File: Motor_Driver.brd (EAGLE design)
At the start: 68.6 x 30.1 mm, 20 parts, among them T1 2N3904, T2 2N3904

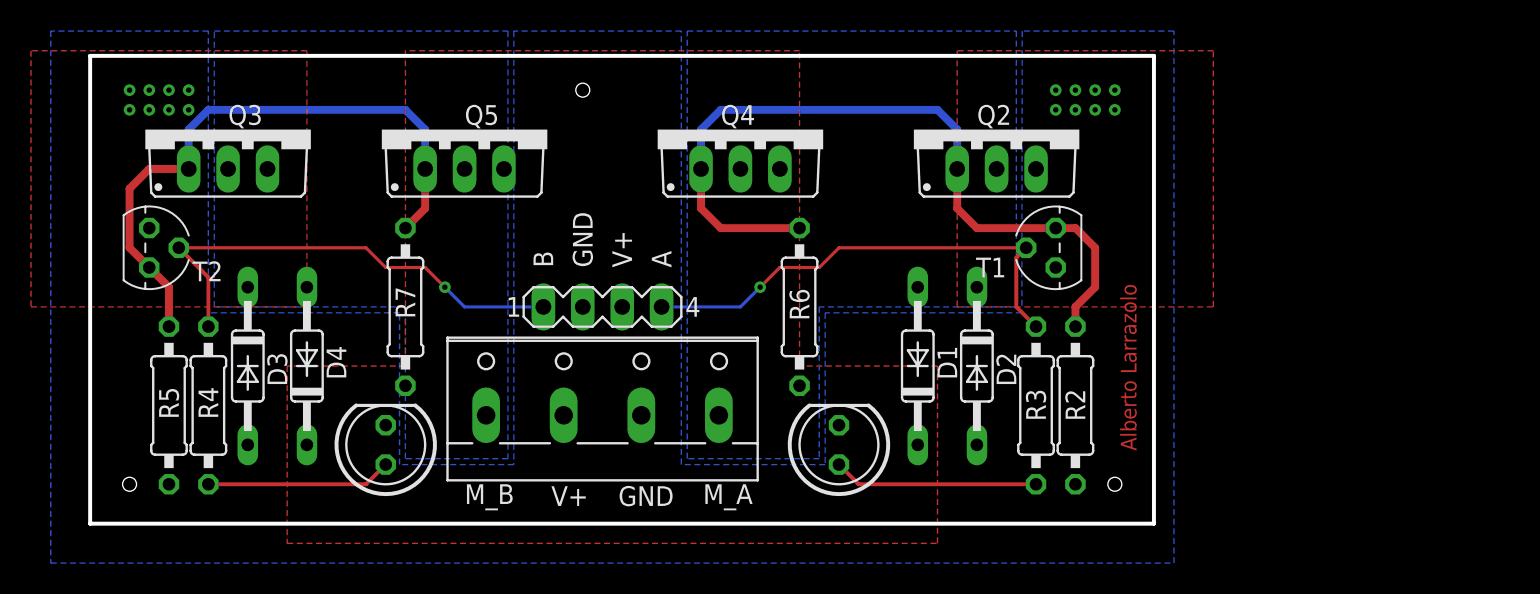
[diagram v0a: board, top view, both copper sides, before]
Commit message: Increased space between MOSFETs to allow for proper heatsink size
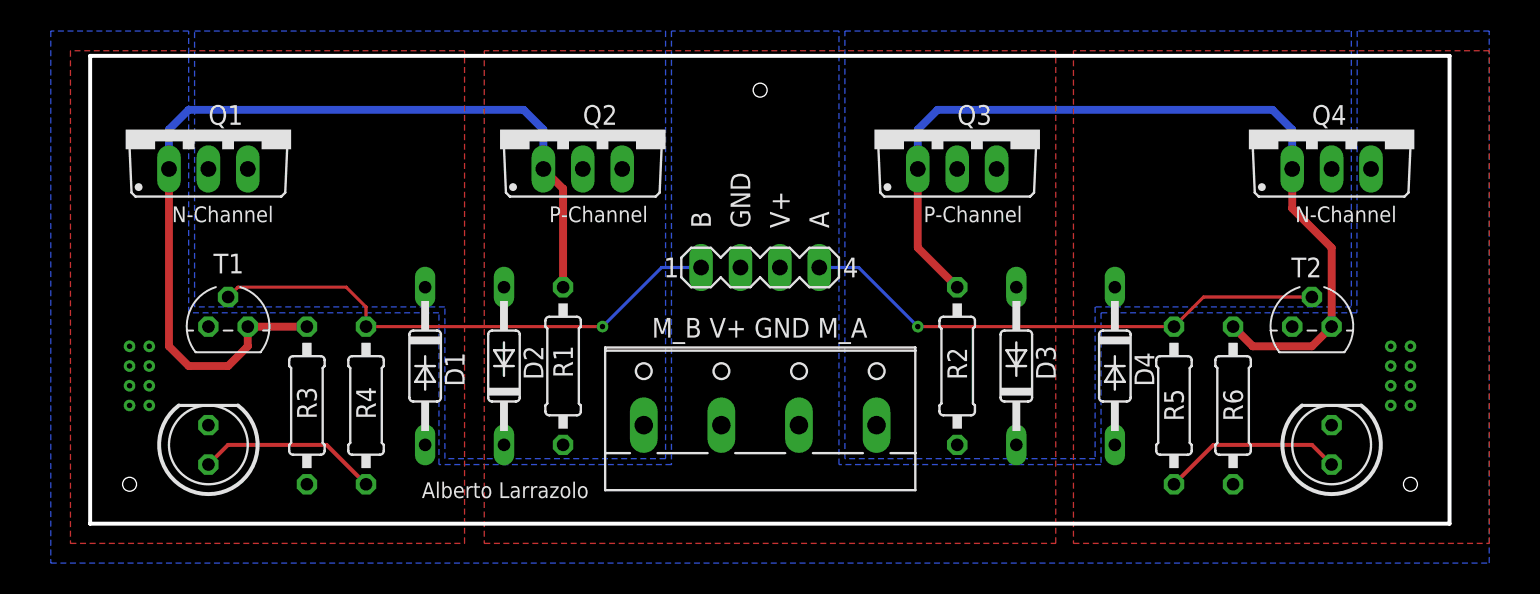
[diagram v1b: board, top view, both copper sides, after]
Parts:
- removed Q5: (no value), transistor-power:TO220BV
- removed R7: 1k, resistor:0207/10
- removed X2: (no value), con-wago-500:W237-4
- added Q1: (no value), transistor-power:TO220BV
- added R1: 1k, resistor:0207/10
- added X1: M_B V+ GND M_A, MyParts:W237-4
- R2, R5: value 10k -> 1k
- R3, R6: value 1k -> 10k
- SV1: value (none) -> INPUT_HEADER; device con-lstb:MA04-1 -> MyParts:MA04-1
- moved T2 75.1 mm to (78.7, 12.7), turned to 0 degrees
- moved R5 64.8 mm to (69.8, 7.62)
- moved LED2 61.0 mm to (80.0, 5.08)
- moved T1 53.6 mm to (8.89, 12.7), turned to 0 degrees
- moved D4 52.1 mm to (66.0, 10.2), turned to 270 degrees
- moved D3 49.5 mm to (59.7, 10.2), turned to 90 degrees
- moved Q3 47.0 mm to (55.9, 25.4)
- moved R3 47.0 mm to (14.0, 7.62)
- moved LED1 40.6 mm to (7.62, 5.08)
- moved Q4 38.1 mm to (80.0, 25.4)
- moved D1 31.8 mm to (21.6, 10.2), turned to 270 degrees
- moved D2 30.5 mm to (26.7, 10.2), turned to 90 degrees
- moved R6 28.7 mm to (73.7, 7.62), turned to 90 degrees
- moved Q2 26.7 mm to (31.8, 25.4)
- moved SV1 10.5 mm to (43.2, 16.5)
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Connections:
- net +12V: now also D2.C, D3.C, Q2.S, Q3.S, R1.2, R2.2, X1.2; no longer D1.C, D4.C, Q4.S, Q5.S, R6.2, R7.2, X2.2
- net DRIVE_A: now also Q3.G, R2.1, R6.2, T2.1; no longer Q2.G, R2.2, R6.1, T1.1
- net DRIVE_B: now also Q1.G, Q2.G, R1.1, R3.2, T1.1; no longer Q3.G, Q5.G, R5.2, R7.1, T2.1
- net GND: now also D1.A, D4.A, Q1.S, Q4.S, R3.1, R6.1, X1.3; no longer D2.A, D3.A, Q2.S, Q3.S, R2.1, R5.1, X2.3
- net INPUT_A: now also R5.2, T2.2; no longer R3.2, T1.2
- net INPUT_B: now also T1.2; no longer T2.2
- net M_DRIVE_A: now also D3.A, D4.C, Q3.D, X1.4; no longer D1.A, D2.C, Q2.D, X2.4
- net M_DRIVE_B: now also D1.C, D2.A, Q1.D, Q2.D, X1.1; no longer D3.C, D4.A, Q3.D, Q5.D, X2.1
- net N$2: now also LED2.A, R5.1; no longer LED1.A, R3.1
- net N$4: now also LED1.A; no longer LED2.A
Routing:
- net DRIVE_B: track 40.0 -> 61.1 mm
- net DRIVE_A: track 50.1 -> 57.5 mm
- net INPUT_B: track 30.8 -> 34.1 mm
- net INPUT_A: track 30.8 -> 34.1 mm
- net N$2: track 13.2 -> 11.7 mm
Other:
- board size 68.6 x 30.1 mm -> 87.6 x 30.1 mm
- board text added: "N-Channel"
- board text added: "P-Channel"

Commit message: Fixed termal relif to allow higher current flow
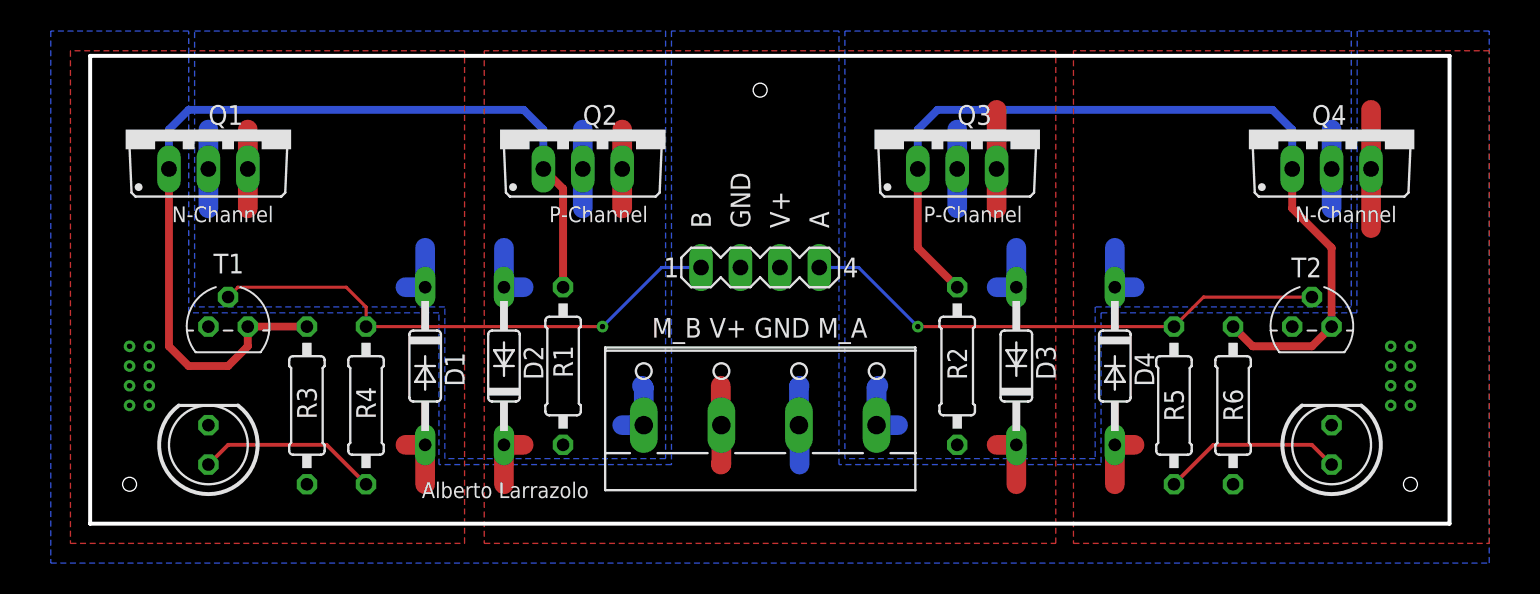
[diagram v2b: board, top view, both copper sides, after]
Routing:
- net GND: track 0.00 -> 25.4 mm
- net +12V: track 0.00 -> 24.2 mm
- net M_DRIVE_B: track 0.00 -> 21.8 mm
- net M_DRIVE_A: track 0.00 -> 21.8 mm
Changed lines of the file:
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@@
 </layers>
 <board>
-<fusionsync huburn="a.cGVyc29uYWw6dWUyYmQxNTYx" projecturn="a.cGVyc29uYWw6dWUyYmQxNTYxIzIwMTcwNTAzNzQ1OTM2NTY" f3durn="urn:adsk.wipprod:dm.lineage:4LoYFpwRT0WNoFuGUnykHQ" pcbguid="78764fb1-ee6b-49c0-b5bc-c6e3655d7beb" lastpulledtime="2019-02-07T21:09:33Z" lastsyncedchangeguid="44b8d85f-1404-02d4-668d-95ffcc52724d"/>
+<fusionsync huburn="a.cGVyc29uYWw6dWUyYmQxNTYx" projecturn="a.cGVyc29uYWw6dWUyYmQxNTYxIzIwMTcwNTAzNzQ1OTM2NTY" f3durn="urn:adsk.wipprod:dm.lineage:4LoYFpwRT0WNoFuGUnykHQ" pcbguid="78764fb1-ee6b-49c0-b5bc-c6e3655d7beb" lastpulledtime="2019-02-07T21:09:33Z" lastsyncedchangeguid="b2fdb641-c53b-a119-a0bc-a5a252d5b16f"/>
 <plain>
 <text x="32.131" y="2.667" size="1.016" layer="21" font="vector" rot="R180">Alberto Larrazolo</text>
@@
 <class number="0" name="default" width="0" drill="0">
 </class>
-<class number="1" name="Motor_Power" width="2.54" drill="0">
+<class number="1" name="Motor_Power" width="1.27" drill="0">
 </class>
 </classes>
@@
 </polygon>
 <contactref element="X1" pad="1"/>
+<wire x1="7.62" y1="22.86" x2="7.62" y2="20.32" width="1.27" layer="16"/>
+<wire x1="7.62" y1="22.86" x2="7.62" y2="25.4" width="1.27" layer="16"/>
+<wire x1="31.75" y1="22.86" x2="31.75" y2="20.32" width="1.27" layer="16"/>
+<wire x1="31.75" y1="22.86" x2="31.75" y2="25.4" width="1.27" layer="16"/>
+<wire x1="35.68" y1="6.35" x2="35.68" y2="8.77" width="1.27" layer="16"/>
+<wire x1="35.68" y1="8.77" x2="35.56" y2="8.89" width="1.27" layer="16"/>
+<wire x1="35.68" y1="6.35" x2="34.29" y2="6.35" width="1.27" layer="16"/>
+<wire x1="21.59" y1="15.24" x2="21.59" y2="17.78" width="1.27" layer="16"/>
+<wire x1="26.67" y1="15.24" x2="27.94" y2="15.24" width="1.27" layer="16"/>
+<wire x1="26.67" y1="15.24" x2="26.67" y2="17.78" width="1.27" layer="16"/>
+<wire x1="21.59" y1="15.24" x2="20.32" y2="15.24" width="1.27" layer="16"/>
 </signal>
 <signal name="M_DRIVE_A" class="1">
@@
 </polygon>
 <contactref element="X1" pad="4"/>
+<wire x1="55.88" y1="22.86" x2="55.88" y2="20.32" width="1.27" layer="16"/>
+<wire x1="55.88" y1="22.86" x2="55.88" y2="25.4" width="1.27" layer="16"/>
+<wire x1="80.01" y1="22.86" x2="80.01" y2="25.4" width="1.27" layer="16"/>
+<wire x1="80.01" y1="22.86" x2="80.01" y2="20.32" width="1.27" layer="16"/>
+<wire x1="50.68" y1="6.35" x2="50.68" y2="8.77" width="1.27" layer="16"/>
+<wire x1="50.68" y1="8.77" x2="50.8" y2="8.89" width="1.27" layer="16"/>
+<wire x1="50.68" y1="6.35" x2="52.07" y2="6.35" width="1.27" layer="16"/>
+<wire x1="66.04" y1="15.24" x2="67.31" y2="15.24" width="1.27" layer="16"/>
+<wire x1="66.04" y1="15.24" x2="66.04" y2="17.78" width="1.27" layer="16"/>
+<wire x1="59.69" y1="15.24" x2="58.42" y2="15.24" width="1.27" layer="16"/>
+<wire x1="59.69" y1="15.24" x2="59.69" y2="17.78" width="1.27" layer="16"/>
 </signal>
 <signal name="+12V">
@@
 <contactref element="D2" pad="C"/>
 <contactref element="X1" pad="2"/>
+<wire x1="34.29" y1="22.86" x2="34.29" y2="20.32" width="1.27" layer="1"/>
+<wire x1="34.29" y1="22.86" x2="34.29" y2="25.4" width="1.27" layer="1"/>
+<wire x1="58.42" y1="22.86" x2="58.42" y2="20.32" width="1.27" layer="1"/>
+<wire x1="58.42" y1="22.86" x2="58.42" y2="26.67" width="1.27" layer="1"/>
+<wire x1="40.68" y1="6.35" x2="40.64" y2="6.39" width="1.27" layer="1"/>
+<wire x1="40.64" y1="6.39" x2="40.64" y2="8.89" width="1.27" layer="1"/>
+<wire x1="40.68" y1="6.35" x2="40.68" y2="3.85" width="1.27" layer="1"/>
+<wire x1="40.68" y1="3.85" x2="40.64" y2="3.81" width="1.27" layer="1"/>
+<wire x1="26.67" y1="5.08" x2="26.67" y2="2.54" width="1.27" layer="1"/>
+<wire x1="26.67" y1="5.08" x2="27.94" y2="5.08" width="1.27" layer="1"/>
+<wire x1="59.69" y1="5.08" x2="58.42" y2="5.08" width="1.27" layer="1"/>
+<wire x1="59.69" y1="5.08" x2="59.69" y2="2.54" width="1.27" layer="1"/>
 </signal>
 <signal name="GND">
@@
 <via x="83.82" y="11.43" extent="1-16" drill="0.35"/>
 <contactref element="X1" pad="3"/>
+<wire x1="82.55" y1="22.86" x2="82.55" y2="19.05" width="1.27" layer="1"/>
+<wire x1="82.55" y1="22.86" x2="82.55" y2="26.67" width="1.27" layer="1"/>
+<wire x1="10.16" y1="22.86" x2="10.16" y2="20.32" width="1.27" layer="1"/>
+<wire x1="10.16" y1="22.86" x2="10.16" y2="25.4" width="1.27" layer="1"/>
+<wire x1="45.68" y1="6.35" x2="45.68" y2="8.85" width="1.27" layer="16"/>
+<wire x1="45.68" y1="8.85" x2="45.72" y2="8.89" width="1.27" layer="16"/>
+<wire x1="45.68" y1="6.35" x2="45.72" y2="6.31" width="1.27" layer="16"/>
+<wire x1="45.72" y1="6.31" x2="45.72" y2="3.81" width="1.27" layer="16"/>
+<wire x1="21.59" y1="5.08" x2="21.59" y2="2.54" width="1.27" layer="1"/>
+<wire x1="21.59" y1="5.08" x2="20.32" y2="5.08" width="1.27" layer="1"/>
+<wire x1="66.04" y1="5.08" x2="66.04" y2="2.54" width="1.27" layer="1"/>
+<wire x1="66.04" y1="5.08" x2="67.31" y2="5.08" width="1.27" layer="1"/>
 </signal>
 <signal name="INPUT_A">

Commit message: Fixed a trace that had shallow angle.
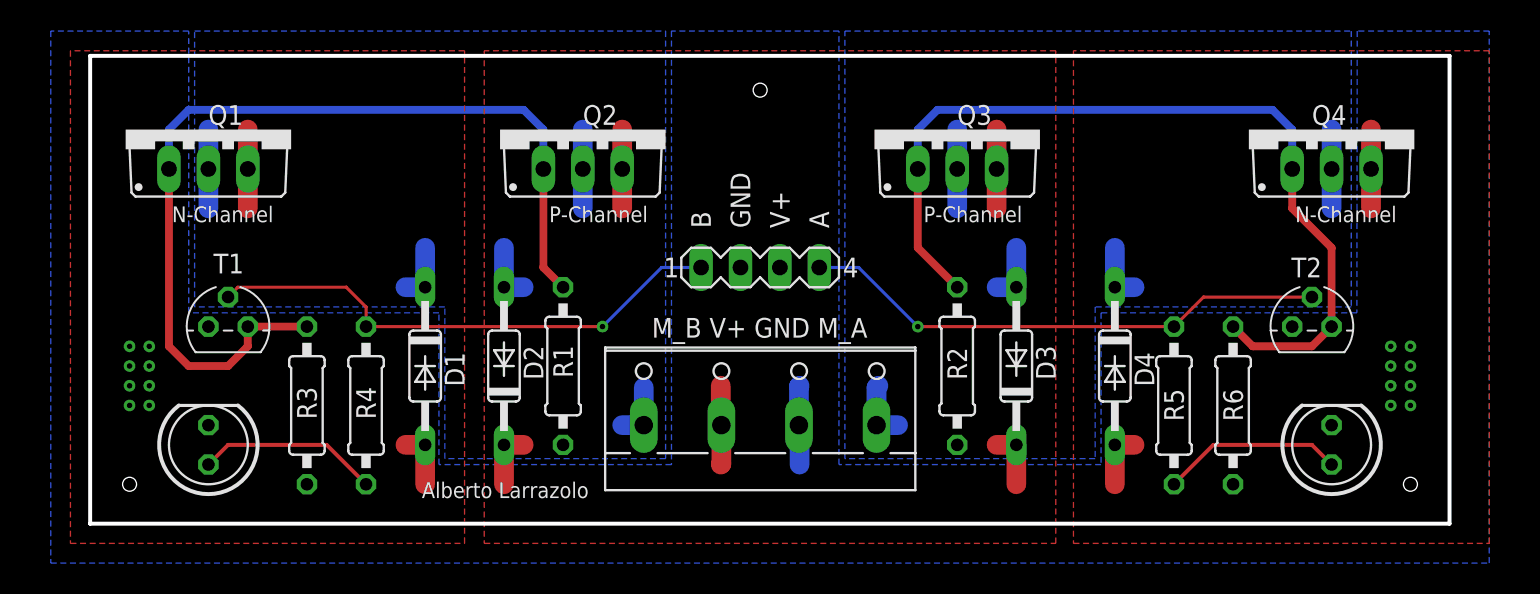
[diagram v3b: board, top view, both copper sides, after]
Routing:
- net GND: track 25.4 -> 22.9 mm
- net +12V: track 24.2 -> 22.9 mm
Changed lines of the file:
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@@
 <contactref element="Q1" pad="G"/>
 <contactref element="Q2" pad="G"/>
-<wire x1="29.21" y1="22.86" x2="30.48" y2="21.59" width="0.508" layer="1"/>
-<wire x1="30.48" y1="21.59" x2="30.48" y2="15.24" width="0.508" layer="1"/>
+<wire x1="29.21" y1="22.86" x2="29.21" y2="16.51" width="0.508" layer="1"/>
+<wire x1="29.21" y1="16.51" x2="30.48" y2="15.24" width="0.508" layer="1"/>
 <wire x1="6.35" y1="26.67" x2="5.08" y2="25.4" width="0.508" layer="16"/>
 <wire x1="5.08" y1="25.4" x2="5.08" y2="22.86" width="0.508" layer="16"/>
@@
 <wire x1="31.75" y1="22.86" x2="31.75" y2="25.4" width="1.27" layer="16"/>
 <wire x1="35.68" y1="6.35" x2="35.68" y2="8.77" width="1.27" layer="16"/>
-<wire x1="35.68" y1="8.77" x2="35.56" y2="8.89" width="1.27" layer="16"/>
 <wire x1="35.68" y1="6.35" x2="34.29" y2="6.35" width="1.27" layer="16"/>
 <wire x1="21.59" y1="15.24" x2="21.59" y2="17.78" width="1.27" layer="16"/>
@@
 <wire x1="34.29" y1="22.86" x2="34.29" y2="25.4" width="1.27" layer="1"/>
 <wire x1="58.42" y1="22.86" x2="58.42" y2="20.32" width="1.27" layer="1"/>
-<wire x1="58.42" y1="22.86" x2="58.42" y2="26.67" width="1.27" layer="1"/>
+<wire x1="58.42" y1="22.86" x2="58.42" y2="25.4" width="1.27" layer="1"/>
 <wire x1="40.68" y1="6.35" x2="40.64" y2="6.39" width="1.27" layer="1"/>
 <wire x1="40.64" y1="6.39" x2="40.64" y2="8.89" width="1.27" layer="1"/>
@@
 <via x="83.82" y="11.43" extent="1-16" drill="0.35"/>
 <contactref element="X1" pad="3"/>
-<wire x1="82.55" y1="22.86" x2="82.55" y2="19.05" width="1.27" layer="1"/>
-<wire x1="82.55" y1="22.86" x2="82.55" y2="26.67" width="1.27" layer="1"/>
+<wire x1="82.55" y1="22.86" x2="82.55" y2="20.32" width="1.27" layer="1"/>
+<wire x1="82.55" y1="22.86" x2="82.55" y2="25.4" width="1.27" layer="1"/>
 <wire x1="10.16" y1="22.86" x2="10.16" y2="20.32" width="1.27" layer="1"/>
 <wire x1="10.16" y1="22.86" x2="10.16" y2="25.4" width="1.27" layer="1"/>
